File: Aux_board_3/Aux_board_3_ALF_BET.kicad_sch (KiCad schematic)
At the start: 37 parts, among them Q10 BSS84KJ, Q11 BSS138KJ, Q12 BSS84KJ, Q13 BSS138KJ, Q14 BSS84KJ, Q15 BSS138KJ, Q16 BSS84KJ, Q7 BSS138KJ, Q8 BSS84KJ, Q9 BSS138KJ

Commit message: finished Board 3 schematic
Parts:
- removed Q10, Q12, Q14, Q16, Q8: BSS84KJ, Package_TO_SOT_SMD:SOT-23, symbol Transistor_FET:BSS84
- removed Q11, Q13, Q15, Q7, Q9: BSS138KJ, Package_TO_SOT_SMD:SOT-23, symbol Transistor_FET:BSS138
- removed R23, R29, R35, R41: 4k7, Resistor_SMD:R_0805_2012Metric_Pad1.20x1.40mm_HandSolder, symbol Device:R
- removed R24, R25, R30, R31, R36, R37, R42, R43: 560R, Resistor_SMD:R_0805_2012Metric_Pad1.20x1.40mm_HandSolder, symbol Device:R
- removed R26, R27, R28, R32, R33, R34, R38, R39, R40, R44, R45: 0R, Resistor_SMD:R_0805_2012Metric_Pad1.20x1.40mm_HandSolder, symbol Device:R
- added Q17, Q19, Q21, Q23, Q25, Q27, Q29, Q31: BSS138KJ, Package_TO_SOT_SMD:SOT-23, symbol Transistor_FET:BSS138
- added Q18, Q20, Q22, Q24, Q26, Q28, Q30, Q32: BSS84KJ, Package_TO_SOT_SMD:SOT-23, symbol Transistor_FET:BSS84
- added R50, R51, R53, R54, R56, R57, R59, R60, R62, R63, R65, R66, R68, R69: 560R, Resistor_SMD:R_0805_2012Metric_Pad1.20x1.40mm_HandSolder, symbol Device:R
- added R52, R55, R58, R61, R64, R67: 4k7, Resistor_SMD:R_0805_2012Metric_Pad1.20x1.40mm_HandSolder, symbol Device:R
- R46: value 0R -> 4k7; Sourced 0 -> 1; Supplier LCSC -> Lomex; Supplier URL https://www.lcsc.com/product-detail/Chip-Resistor-Surface-M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 -> (none); Supplier item no C304192 -> 81-10-95; now fitted
- R47: value 4k7 -> 560R; Supplier item no 81-10-95 -> 81-10-84
- R49: value 560R -> 4k7; Supplier item no 81-10-84 -> 81-10-95
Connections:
- net TH_HOME_NG is gone; now on net GND: R48.2
- net TH_HOME_PG is gone; now on net +24V: R47.1
- net +24V: now also Q18.3 (D), Q20.3 (D), Q22.3 (D), Q24.3 (D), Q26.3 (D), Q28.3 (D), Q30.3 (D), Q32.3 (D), R50.1, R53.1, R56.1, R59.1, R62.1, R65.1, R68.1; no longer R48.1
- net GND: now also Q17.2 (S), Q19.2 (S), Q21.2 (S), Q23.2 (S), Q25.2 (S), Q27.2 (S), Q29.2 (S), Q31.2 (S), R51.2, R54.2, R57.2, R60.2, R63.2, R66.2, R69.2; no longer R49.2
- net +3V3 renamed ALF_ENC_A_NG
- net ALF_ENC_A_NG: now also Q17.1 (G)
- net TH_HOME renamed ALF_ENC_B_NG
- net ALF_ENC_B_NG: now also Q19.1 (G)
- net TH_HOME_IN renamed ALF_ENC_A_PG
- net ALF_ENC_A_PG: now also Q17.3 (D), Q18.1 (G)
- net TH_HOME_PWR renamed ALF_ENC_A_IN
- new net ALF_ENC_A: Q18.2 (S), R48.1
- new net ALF_ENC_B: Q20.2 (S), R51.1
- new net ALF_ENC_B_IN: R49.2
- new net ALF_LIM_MAX: Q24.2 (S), R57.1
- new net ALF_LIM_MAX_IN: R55.2
- new net ALF_LIM_MAX_NG: Q23.1 (G), R55.1
- new net ALF_LIM_MAX_PG: Q23.3 (D), Q24.1 (G), R56.2
- new net ALF_LIM_MIN: Q22.2 (S), R54.1
- new net ALF_LIM_MIN_IN: R52.2
- new net ALF_LIM_MIN_NG: Q21.1 (G), R52.1
- new net ALF_LIM_MIN_PG: Q21.3 (D), Q22.1 (G), R53.2
- new net BET_ENC_A: Q26.2 (S), R60.1
- new net BET_ENC_A_IN: R58.2
- new net BET_ENC_A_NG: Q25.1 (G), R58.1
- new net BET_ENC_A_PG: Q25.3 (D), Q26.1 (G), R59.2
- new net BET_ENC_B: Q28.2 (S), R63.1
- new net BET_ENC_B_IN: R61.2
- new net BET_ENC_B_NG: Q27.1 (G), R61.1
- new net BET_LIM_MAX: Q32.2 (S), R69.1
- new net BET_LIM_MAX_IN: R67.2
- new net BET_LIM_MAX_NG: Q31.1 (G), R67.1
- new net BET_LIM_MAX_PG: Q31.3 (D), Q32.1 (G), R68.2
- new net BET_LIM_MIN: Q30.2 (S), R66.1
- new net BET_LIM_MIN_IN: R64.2
- new net BET_LIM_MIN_NG: Q29.1 (G), R64.1
- new net BET_LIM_MIN_PG: Q29.3 (D), Q30.1 (G), R65.2
- new net TN_ENC_B_PG: Q19.3 (D), Q20.1 (G), Q27.3 (D), Q28.1 (G), R50.2, R62.2
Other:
- note added: "Alpha axis sensors level shifting to 24V"
- note added: "Beta axis sensors level shifting to 24V"
- note removed: "THETA axis sensors level shifting to 24V"

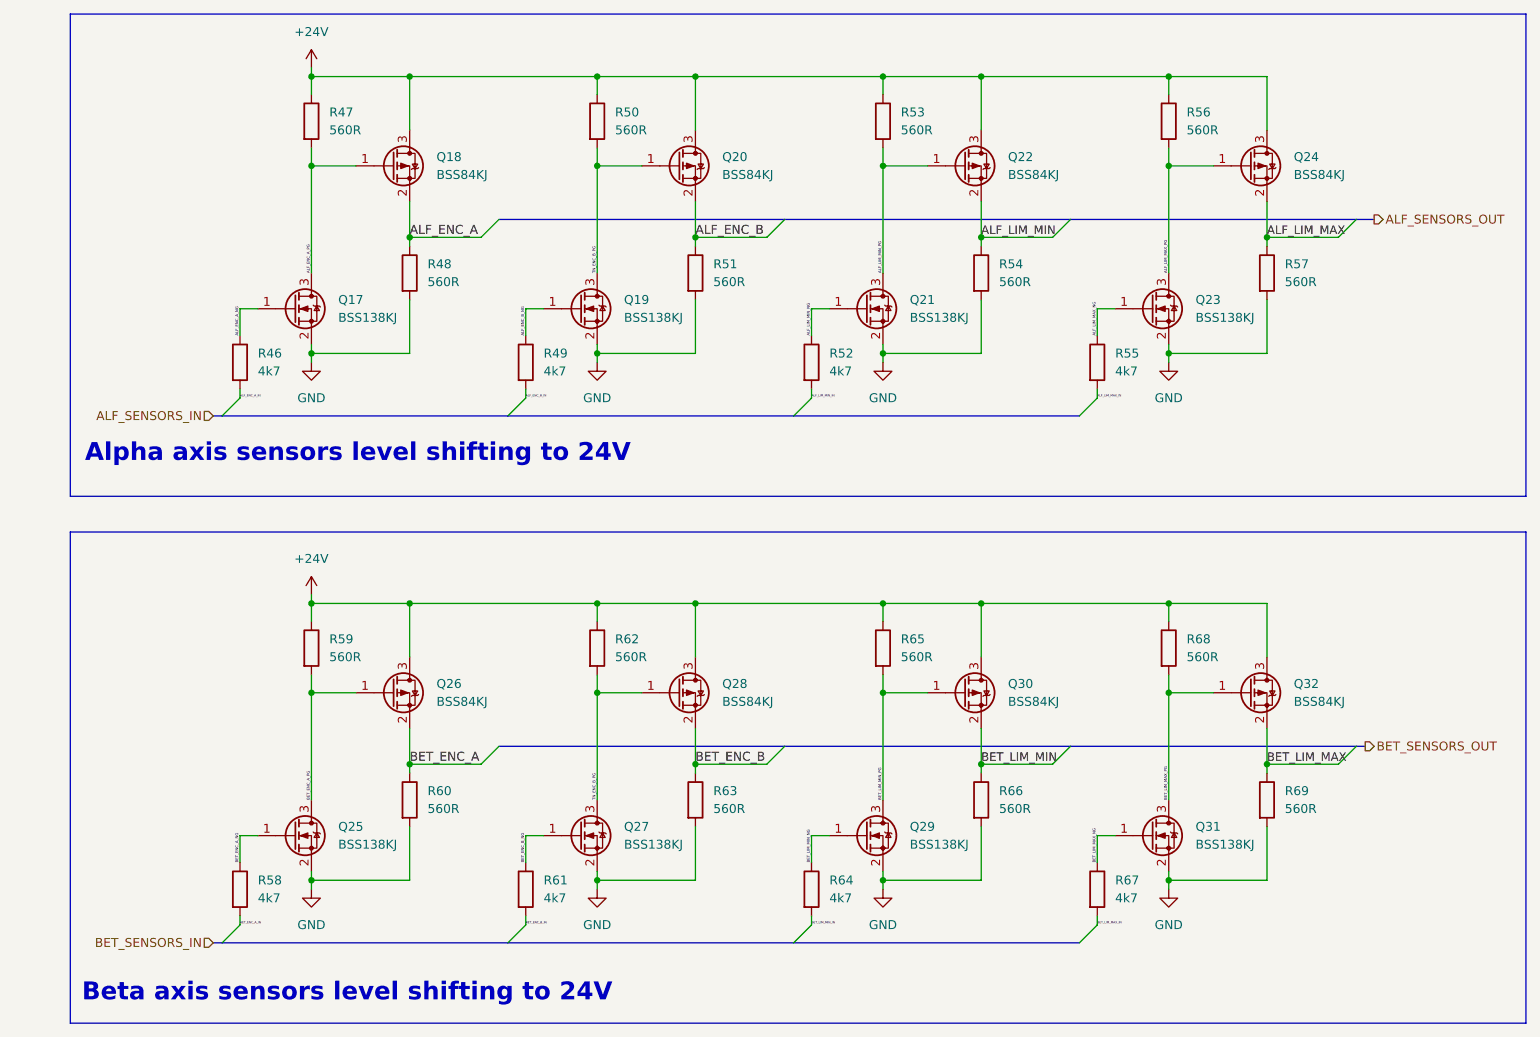
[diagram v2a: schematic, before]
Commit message: Board 3 MODBUS and servos done
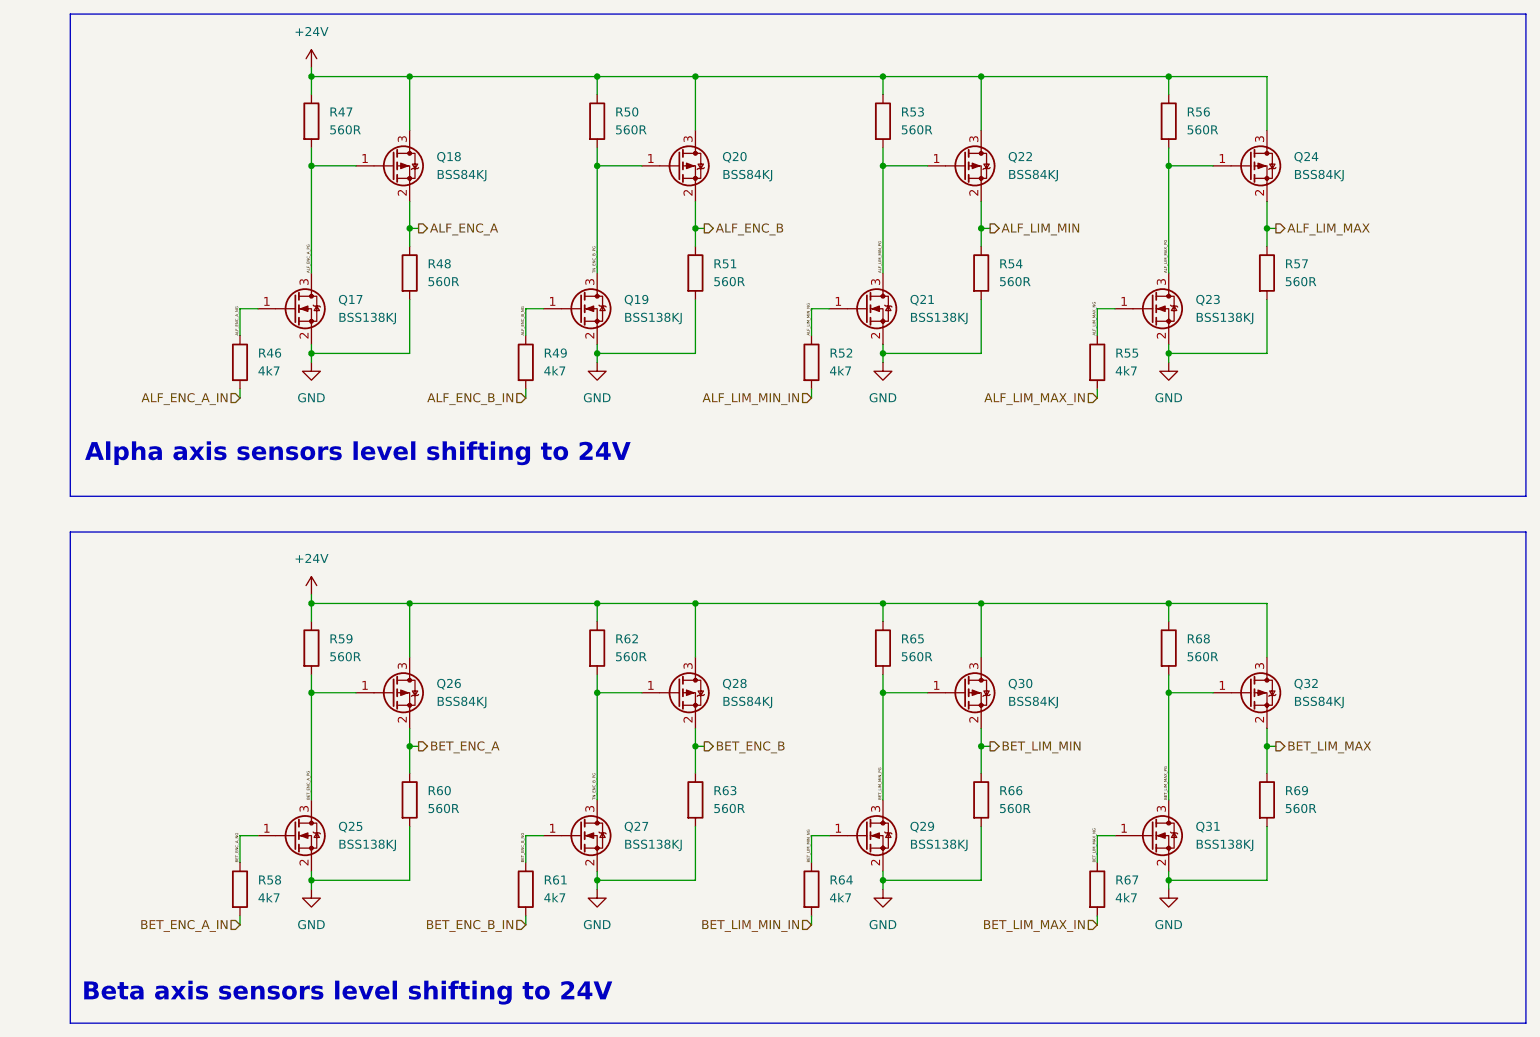
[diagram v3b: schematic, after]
